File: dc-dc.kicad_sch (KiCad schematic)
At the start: 132 parts, among them SW3 CVS-02B, U31 MPM54304GMN, U32 MPM54304GMN, U33 MAX16150AUT+T, U34 NCP451AFCT2G, U35 SN74LVC1G125DBVR, U36 LM3880, U37 MP8869S, U38 TPS7A20185PDQNR, U39 NCP51400MNTXG, U40 XC6230H001ER-G, U41 REF3012AIDBZT

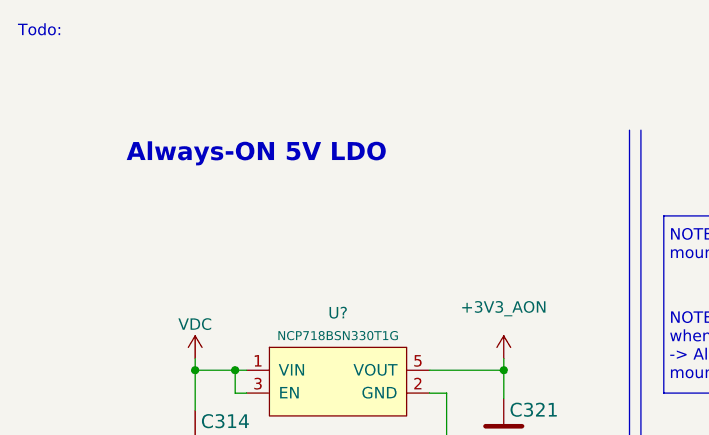
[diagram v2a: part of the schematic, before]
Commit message: Connected USB PON and DET signals to FPGA
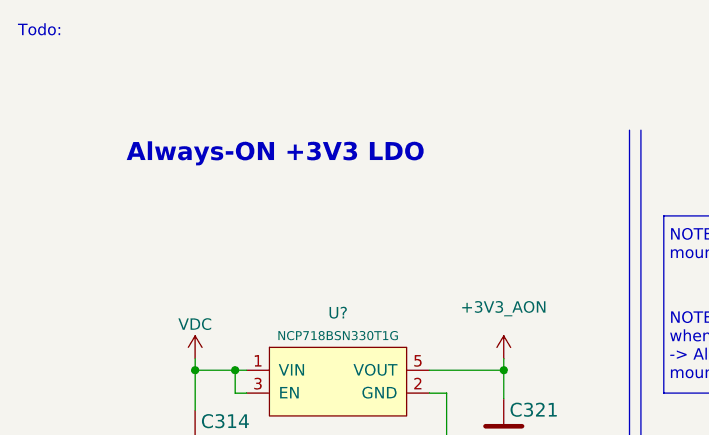
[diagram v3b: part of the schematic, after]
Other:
- note added: "Always-ON +3V3 LDO"
- note removed: "Always-ON 5V LDO"
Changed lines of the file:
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@@
     (effects (font (size 1.27 1.27)) (justify left bottom))
   )
-  (text "Always-ON 5V LDO" (at 13.335 16.51 0)
+  (text "Always-ON +3V3 LDO" (at 13.335 16.51 0)
     (effects (font (size 2 2) (thickness 0.254) bold) (justify left bottom))
   )

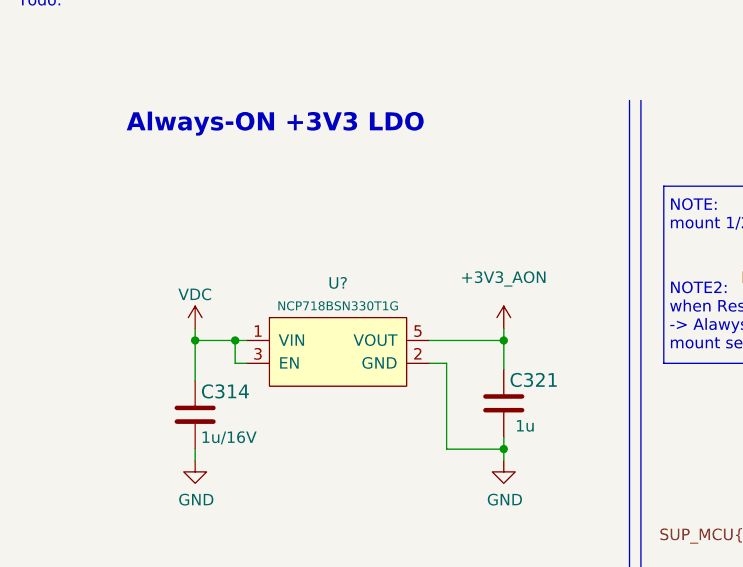
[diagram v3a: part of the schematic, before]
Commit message: Annotated designators for new components
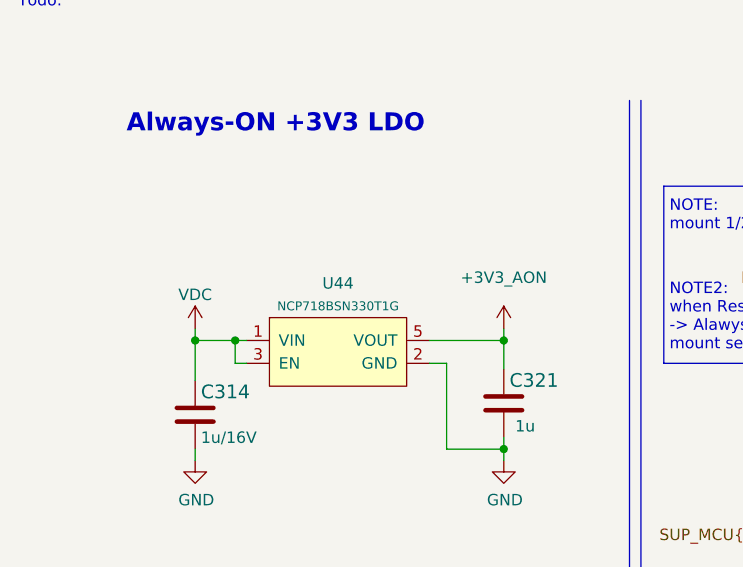
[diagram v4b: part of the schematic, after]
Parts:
- gave numbers to parts that had none: 1
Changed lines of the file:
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@@
   (symbol (lib_id "power:+3V3_AON") (at 127 43.18 0) (unit 1)
     (in_bom yes) (on_board yes) (fields_autoplaced)
-    (property "Reference" "#PWR?" (id 0) (at 127 46.99 0)
+    (property "Reference" "#PWR0473" (id 0) (at 127 46.99 0)
       (effects (font (size 1.27 1.27)) hide)
     )
@@
   (symbol (lib_id "power:+3V3_AON") (at 55.245 38.1 0) (unit 1)
     (in_bom yes) (on_board yes) (fields_autoplaced)
-    (property "Reference" "#PWR?" (id 0) (at 55.245 41.91 0)
+    (property "Reference" "#PWR0472" (id 0) (at 55.245 41.91 0)
       (effects (font (size 1.27 1.27)) hide)
     )
@@
   (symbol (lib_id "antmicroPMICVoltageRegulatorsLinear:NCP718BSN330T1G") (at 36.83 40.64 0) (unit 1)
     (in_bom yes) (on_board yes) (fields_autoplaced)
-    (property "Reference" "U?" (id 0) (at 36.83 33.02 0))
+    (property "Reference" "U44" (id 0) (at 36.83 33.02 0))
     (property "Value" "NCP718BSN330T1G" (id 1) (at 36.83 35.56 0)
       (effects (font (size 0.9906 0.9906)))
@@
   (symbol (lib_id "power:+3V3_AON") (at 168.91 18.415 0) (unit 1)
     (in_bom yes) (on_board yes) (fields_autoplaced)
-    (property "Reference" "#PWR?" (id 0) (at 168.91 22.225 0)
+    (property "Reference" "#PWR0474" (id 0) (at 168.91 22.225 0)
       (effects (font (size 1.27 1.27)) hide)
     )
@@
   (symbol (lib_id "power:+3V3_AON") (at 215.265 31.75 0) (unit 1)
     (in_bom yes) (on_board yes) (fields_autoplaced)
-    (property "Reference" "#PWR?" (id 0) (at 215.265 35.56 0)
-      (effects (font (size 1.27 1.27)) hide)
-    )
+    (property "Reference" "#PWR0475" (id 0) (at 215.265 35.56 0)
+      (effects (font (size 1.27 1.27)) hide)
+    )

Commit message: Loclib
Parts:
- C314: footprint antmicro-footprints:0402-cap -> K410T-devboard-footprints:0402-cap; symbol antmicroCapacitors0402:C_1u_0402_16V -> K410T-devboard:C_1u_0402_16V
- C315, C317, C319, C320, C341, C345: footprint antmicro-footprints:0805-cap -> K410T-devboard-footprints:0805-cap; symbol antmicroCapacitorsmisc:C_22u_0805_25V -> K410T-devboard:C_22u_0805_25V
- C316, C318, C321, C334, C335, C346, C348, C352: footprint antmicro-footprints:0402-cap -> K410T-devboard-footprints:0402-cap; symbol antmicroCapacitors0402:C_1u_0402 -> K410T-devboard:C_1u_0402
- C322, C323, C324, C325, C326, C327, C328, C329, C330, C331, C332, C333, C357, C359, C360, C363: footprint antmicro-footprints:0603-cap -> K410T-devboard-footprints:0603-cap; symbol antmicroCapacitors0603:C_22u_0603 -> K410T-devboard:C_22u_0603
- C336, C337, C338, C339, C343, C347, C351, C356, C362: footprint antmicro-footprints:0402-cap -> K410T-devboard-footprints:0402-cap; symbol antmicroCapacitors0402:C_100n_0402 -> K410T-devboard:C_100n_0402
- C340, C344, C353, C355, C358, C361: footprint antmicro-footprints:0402-cap -> K410T-devboard-footprints:0402-cap; symbol antmicroCapacitors0402:C_10u_0402 -> K410T-devboard:C_10u_0402
- C342: footprint antmicro-footprints:0402-cap -> K410T-devboard-footprints:0402-cap; symbol antmicroCapacitors0402:C_470n_0402 -> K410T-devboard:C_470n_0402
- C349: footprint antmicro-footprints:0201-cap -> K410T-devboard-footprints:0201-cap; symbol antmicroCapacitorsmisc:C_4u7_0201 -> K410T-devboard:C_4u7_0201
- C350: footprint antmicro-footprints:0402-res -> K410T-devboard-footprints:0402-res; symbol antmicroCapacitors0402:C_1n_0402 -> K410T-devboard:C_1n_0402
- C354: footprint antmicro-footprints:0402-cap -> K410T-devboard-footprints:0402-cap; symbol antmicroCapacitors0402:C_22n_0402 -> K410T-devboard:C_22n_0402
- C364: footprint antmicro-footprints:0402-cap -> K410T-devboard-footprints:0402-cap; symbol antmicroCapacitors0402:C_22p_0402 -> K410T-devboard:C_22p_0402
- D33: footprint antmicro-footprints:SOT-23-3 -> K410T-devboard-footprints:SOT-23-3; symbol antmicroDiodesZenerSingle:BZX84C5V1-TP -> K410T-devboard:BZX84C5V1-TP
- FB11: footprint antmicro-footprints:0402-res -> K410T-devboard-footprints:0402-res; symbol antmicroFerriteBeadsandChips:BLM15PD121SN1D -> K410T-devboard:BLM15PD121SN1D
- L1: footprint antmicro-footprints:Bourns-SRP6050CA -> K410T-devboard-footprints:Bourns-SRP6050CA; symbol antmicroFixedInductors: SRP6050CA-1R5M -> K410T-devboard: SRP6050CA-1R5M
- NT1, NT2: footprint antmicro-footprints:NetTie-2_SMD_Pad0.127mm -> K410T-devboard-footprints:NetTie-2_SMD_Pad0.127mm; symbol antmicroShuntsJumpers:NetTie_2 -> K410T-devboard:NetTie_2
- R277: footprint antmicro-footprints:0402-res -> K410T-devboard-footprints:0402-res; symbol antmicroResistors0402:R_510k_0402 -> K410T-devboard:R_510k_0402
- R278: footprint antmicro-footprints:0402-res -> K410T-devboard-footprints:0402-res; symbol antmicroResistors0402:R_330k_0402 -> K410T-devboard:R_330k_0402
- R279, R280, R295, R296, R297, R298, R299, R300, R301, R302, R303, R304, R305, R306, R307, R308, R309, R310, R311, R312, R313, R314, R315, R316, R317, R319, R320, R328, R329: footprint antmicro-footprints:0402-res -> K410T-devboard-footprints:0402-res; symbol antmicroResistors0402:R_0R_0402 -> K410T-devboard:R_0R_0402
- R283, R284, R293, R294, R318, R321, R322: footprint antmicro-footprints:0402-res -> K410T-devboard-footprints:0402-res; symbol antmicroResistors0402:R_47k_0402 -> K410T-devboard:R_47k_0402
- R285, R286, R287, R288, R289, R290, R291, R292, R326, R330, R333, R37: footprint antmicro-footprints:0603-res -> K410T-devboard-footprints:0603-res; symbol antmicroResistors0603:R_0R_0603_HPWR -> K410T-devboard:R_0R_0603_HPWR
- R323, R324, R327: footprint antmicro-footprints:0402-res -> K410T-devboard-footprints:0402-res; symbol antmicroResistors0402:R_10k_0402 -> K410T-devboard:R_10k_0402
- R325: footprint antmicro-footprints:0402-res -> K410T-devboard-footprints:0402-res; symbol antmicroResistors0402:R_4k7_0402 -> K410T-devboard:R_4k7_0402
- R331: footprint antmicro-footprints:0402-res -> K410T-devboard-footprints:0402-res; symbol antmicroResistors0402:R_80k6_0402 -> K410T-devboard:R_80k6_0402
- R332: footprint antmicro-footprints:0402-res -> K410T-devboard-footprints:0402-res; symbol antmicroResistors0402:R_205k_0402 -> K410T-devboard:R_205k_0402
- R341: footprint antmicro-footprints:0402-res -> K410T-devboard-footprints:0402-res; symbol antmicroResistors0402:R_100k_0402 -> K410T-devboard:R_100k_0402
- S6: footprint antmicro-footprints:SW_SPST_4.2x2.8 -> K410T-devboard-footprints:SW_SPST_4.2x2.8; symbol antmicroPushbuttonSwitches:KMR2 -> K410T-devboard:KMR2
- SW3: footprint antmicro-footprints:SW_DIP_SPSTx02_Slide_Copal_CVS-02xB_W5.9mm_P1mm -> K410T-devboard-footprints:SW_DIP_SPSTx02_Slide_Copal_CVS-02xB_W5.9mm_P1mm; symbol antmicroSlideSwitches:CVS-02B -> K410T-devboard:CVS-02B
- TP4, TP5, TP6, TP7, TP8: footprint antmicro-footprints:Testpoint_smd_0_75mm -> K410T-devboard-footprints:Testpoint_smd_0_75mm; symbol antmicroTestPoints:TP_SMD_0_75MM -> K410T-devboard:TP_SMD_0_75MM
- U31, U32: footprint antmicro-footprints:MPS_LGA-33 -> K410T-devboard-footprints:MPS_LGA-33; symbol antmicroPMICVoltageRegulatorsDCDCSwitchingRegulators:MPM54304GMN -> K410T-devboard:MPM54304GMN
- U33: footprint antmicro-footprints:SOT-23-6 -> K410T-devboard-footprints:SOT-23-6; symbol antmicroPMICPowerSequencers:MAX16150AUT+T -> K410T-devboard:MAX16150AUT+T
- U34: footprint antmicro-footprints:Onsemi_WLCSP6_1.40x0.90 -> K410T-devboard-footprints:Onsemi_WLCSP6_1.40x0.90; symbol antmicroPMICPowerDistributionSwitchesLoadDrivers:NCP451AFCT2G -> K410T-devboard:NCP451AFCT2G
- U35: footprint antmicro-footprints:SOT-753 -> K410T-devboard-footprints:SOT-753; symbol antmicroLogicBuffersDriversReceiversTransceivers:SN74LVC1G125DBVR -> K410T-devboard:SN74LVC1G125DBVR
- U36: footprint antmicro-footprints:SOT-23-6 -> K410T-devboard-footprints:SOT-23-6; symbol antmicroPMICPowerSequencers:LM3880 -> K410T-devboard:LM3880
- U37: footprint antmicro-footprints:MPS_QFN-14_MP8869S -> K410T-devboard-footprints:MPS_QFN-14_MP8869S; symbol antmicroPMICVoltageRegulatorsDCDCSwitchingRegulators:MP8869S -> K410T-devboard:MP8869S
- U38: footprint antmicro-footprints:XDFN4 -> K410T-devboard-footprints:XDFN4; symbol antmicroPMICVoltageRegulatorsLinear:TPS7A20185PDQNR -> K410T-devboard:TPS7A20185PDQNR
- U39: footprint antmicro-footprints:DFN-10-1EP_3x3mm -> K410T-devboard-footprints:DFN-10-1EP_3x3mm; symbol antmicroPMICVoltageRegulatorsDCDCSwitchingControllers:NCP51400MNTXG -> K410T-devboard:NCP51400MNTXG
- U40: footprint antmicro-footprints:Torex_USP-6C -> K410T-devboard-footprints:Torex_USP-6C; symbol antmicroPMICVoltageRegulatorsLinear:XC6230H001ER-G -> K410T-devboard:XC6230H001ER-G
- U41: footprint antmicro-footprints:SOT-23-3 -> K410T-devboard-footprints:SOT-23-3; symbol antmicroPMICPowerDistributionSwitchesLoadDrivers:REF3012AIDBZT -> K410T-devboard:REF3012AIDBZT
- U44: footprint antmicro-footprints:SOT-23-5 -> K410T-devboard-footprints:SOT-23-5; symbol antmicroPMICVoltageRegulatorsLinear:NCP718BSN330T1G -> K410T-devboard:NCP718BSN330T1G
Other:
- note added: "1t2t3t4"
- note removed: "1 2 3 4"

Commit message: Finished FMC signals routing
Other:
- note added: "1 2 3 4"
- note removed: "1t2t3t4"
